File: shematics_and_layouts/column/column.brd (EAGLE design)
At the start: 160 x 100 mm, 1 part

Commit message: TASK: col shematic
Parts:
- removed U$1: RPI-ZERO, rpi-zero-without-test-pad:RASP_PI_ZERO_BOARD_FULL
- added A1: RPI-ZERO, rpi-zero-without-test-pad:RASP_PI_ZERO_BOARD_FULL
- added X1: (no value), con-conrad:733980-62
- added X2: (no value), con-berg:PN87520
- added X3: (no value), con-lsta:FE05-2
- added X5: LEDs, con-lstb:MA03-1
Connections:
- new net 3V3@1: A1.1, X3.5
- new net GND: X1.2, X1.3, X2.4, X5.3
- new net GND@3: A1.25, A1.39, A1.9
- new net GND@7: A1.14, A1.20, A1.30, A1.34, A1.6, X3.6
- new net N$1: A1.5, X3.2
- new net N$2: A1.3, X3.4
- new net N$3: A1.12, X5.2
- new net VCC: X1.1, X2.1, X5.1
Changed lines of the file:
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@@
 </autorouter>
 <elements>
-<element name="U$1" library="rpi-zero-without-test-pad" package="RASP_PI_ZERO_BOARD_FULL" value="RPI-ZERO" x="29.21" y="31.75"/>
+<element name="A1" library="rpi-zero-without-test-pad" package="RASP_PI_ZERO_BOARD_FULL" value="RPI-ZERO" x="-69.85" y="67.31"/>
+<element name="X1" library="con-conrad" package="733980-62" value="" x="3.81" y="-2.54"/>
+<element name="X2" library="con-berg" package="PN87520" value="" x="35.56" y="8.89">
+<attribute name="OC_NEWARK" value="unknown" x="35.56" y="8.89" size="1.778" layer="27" display="off"/>
+<attribute name="MPN" value="" x="35.56" y="8.89" size="1.778" layer="27" display="off"/>
+<attribute name="MF" value="" x="35.56" y="8.89" size="1.778" layer="27" display="off"/>
+<attribute name="OC_FARNELL" value="unknown" x="35.56" y="8.89" size="1.778" layer="27" display="off"/>
+</element>
+<element name="X3" library="con-lsta" package="FE05-2" value="" x="-24.13" y="44.45">
+<attribute name="OC_NEWARK" value="unknown" x="-24.13" y="44.45" size="1.778" layer="27" display="off"/>
+<attribute name="MPN" value="" x="-24.13" y="44.45" size="1.778" layer="27" display="off"/>
+<attribute name="MF" value="" x="-24.13" y="44.45" size="1.778" layer="27" display="off"/>
+<attribute name="OC_FARNELL" value="unknown" x="-24.13" y="44.45" size="1.778" layer="27" display="off"/>
+</element>
+<element name="X5" library="con-lstb" package="MA03-1" value="LEDs" x="-64.77" y="-11.43">
+<attribute name="OC_NEWARK" value="unknown" x="-64.77" y="-11.43" size="1.778" layer="27" display="off"/>
+<attribute name="MPN" value="" x="-64.77" y="-11.43" size="1.778" layer="27" display="off"/>
+<attribute name="MF" value="" x="-64.77" y="-11.43" size="1.778" layer="27" display="off"/>
+<attribute name="OC_FARNELL" value="unknown" x="-64.77" y="-11.43" size="1.778" layer="27" display="off"/>
+</element>
 </elements>
 <signals>
+<signal name="VCC">
+<contactref element="X1" pad="1"/>
+<contactref element="X2" pad="1"/>
+<contactref element="X5" pad="1"/>
+<wire x1="3.81" y1="6.03" x2="-67.31" y2="-11.43" width="0" layer="19" extent="1-1"/>
+<wire x1="32.06" y1="11.6" x2="3.81" y2="6.03" width="0" layer="19" extent="1-1"/>
+</signal>
+<signal name="GND">
+<contactref element="X1" pad="3"/>
+<contactref element="X1" pad="2"/>
+<contactref element="X2" pad="4"/>
+<contactref element="X5" pad="3"/>
+<wire x1="3.81" y1="-0.12" x2="-62.23" y2="-11.43" width="0" layer="19" extent="1-1"/>
+<wire x1="8.81" y1="3.03" x2="3.81" y2="-0.12" width="0" layer="19" extent="1-1"/>
+<wire x1="39.06" y1="11.6" x2="8.81" y2="3.03" width="0" layer="19" extent="1-1"/>
+</signal>
+<signal name="N$1">
+<contactref element="X3" pad="2"/>
+<contactref element="A1" pad="5"/>
+<wire x1="-56.4" y1="92.54" x2="-29.21" y2="43.18" width="0" layer="19" extent="1-1"/>
+</signal>
+<signal name="N$2">
+<contactref element="X3" pad="4"/>
+<contactref element="A1" pad="3"/>
+<wire x1="-58.94" y1="92.54" x2="-26.67" y2="43.18" width="0" layer="19" extent="1-1"/>
+</signal>
+<signal name="3V3@1">
+<contactref element="X3" pad="5"/>
+<contactref element="A1" pad="1"/>
+<wire x1="-61.48" y1="92.54" x2="-24.13" y2="45.72" width="0" layer="19" extent="1-1"/>
+</signal>
+<signal name="N$3">
+<contactref element="A1" pad="12"/>
+<contactref element="X5" pad="2"/>
+<wire x1="-48.78" y1="95.08" x2="-64.77" y2="-11.43" width="0" layer="19" extent="1-1"/>
+</signal>
+<signal name="GND@3">
+<contactref element="A1" pad="9"/>
+<contactref element="A1" pad="25"/>
+<contactref element="A1" pad="39"/>
+<wire x1="-31" y1="92.54" x2="-13.22" y2="92.54" width="0" layer="19" extent="1-1"/>
+<wire x1="-51.32" y1="92.54" x2="-31" y2="92.54" width="0" layer="19" extent="1-1"/>
+</signal>
+<signal name="GND@7">
+<contactref element="X3" pad="6"/>
+<contactref element="A1" pad="6"/>
+<contactref element="A1" pad="14"/>
+<contactref element="A1" pad="20"/>
+<contactref element="A1" pad="30"/>
+<contactref element="A1" pad="34"/>
+<wire x1="-25.92" y1="95.08" x2="-20.84" y2="95.08" width="0" layer="19" extent="1-1"/>
+<wire x1="-38.62" y1="95.08" x2="-25.92" y2="95.08" width="0" layer="19" extent="1-1"/>
+<wire x1="-46.24" y1="95.08" x2="-38.62" y2="95.08" width="0" layer="19" extent="1-1"/>
+<wire x1="-56.4" y1="95.08" x2="-46.24" y2="95.08" width="0" layer="19" extent="1-1"/>
+<wire x1="-24.13" y1="43.18" x2="-25.92" y2="95.08" width="0" layer="19" extent="1-1"/>
+</signal>
 </signals>
 </board>

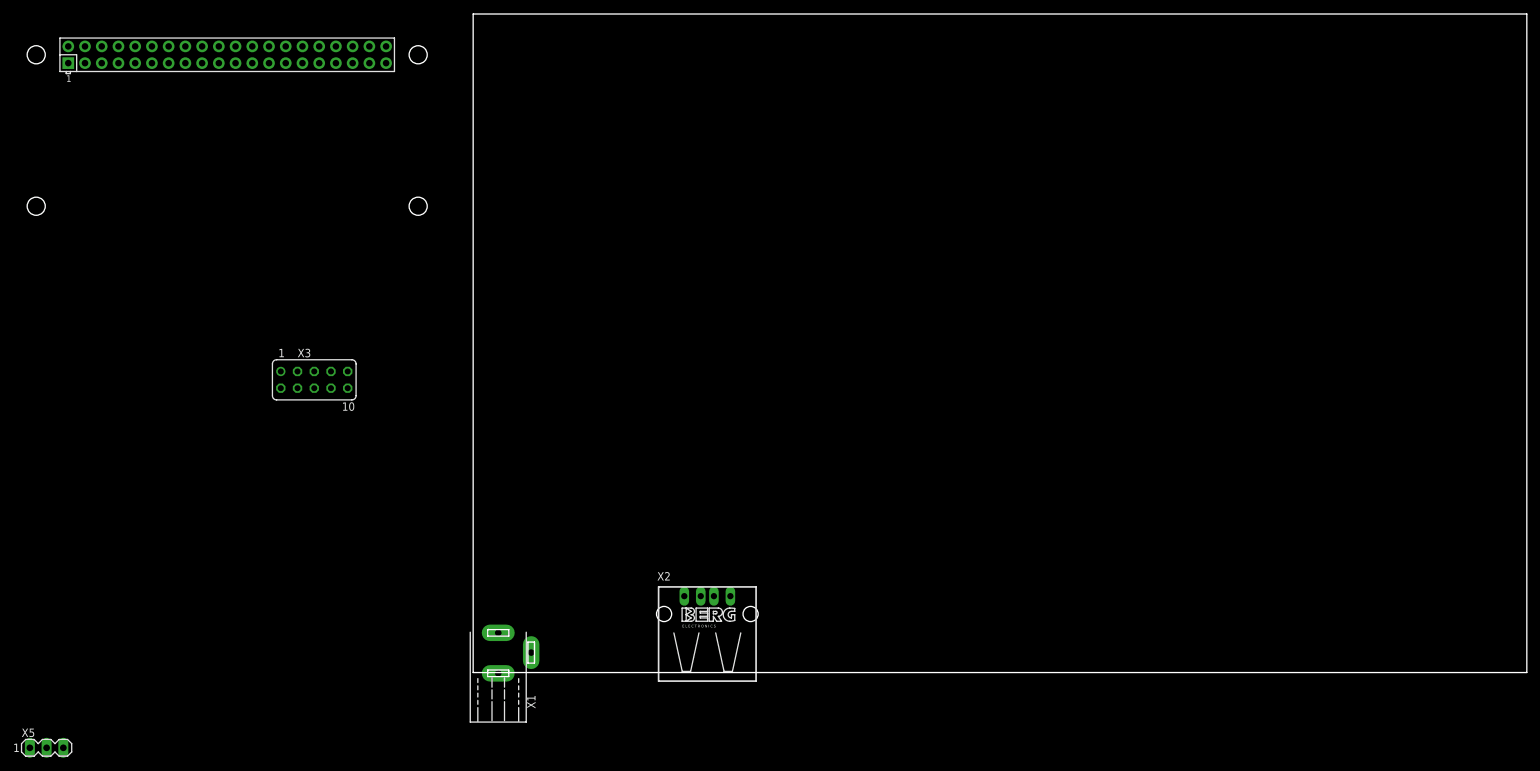
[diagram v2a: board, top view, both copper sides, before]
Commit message: TASK: col brd, part placement
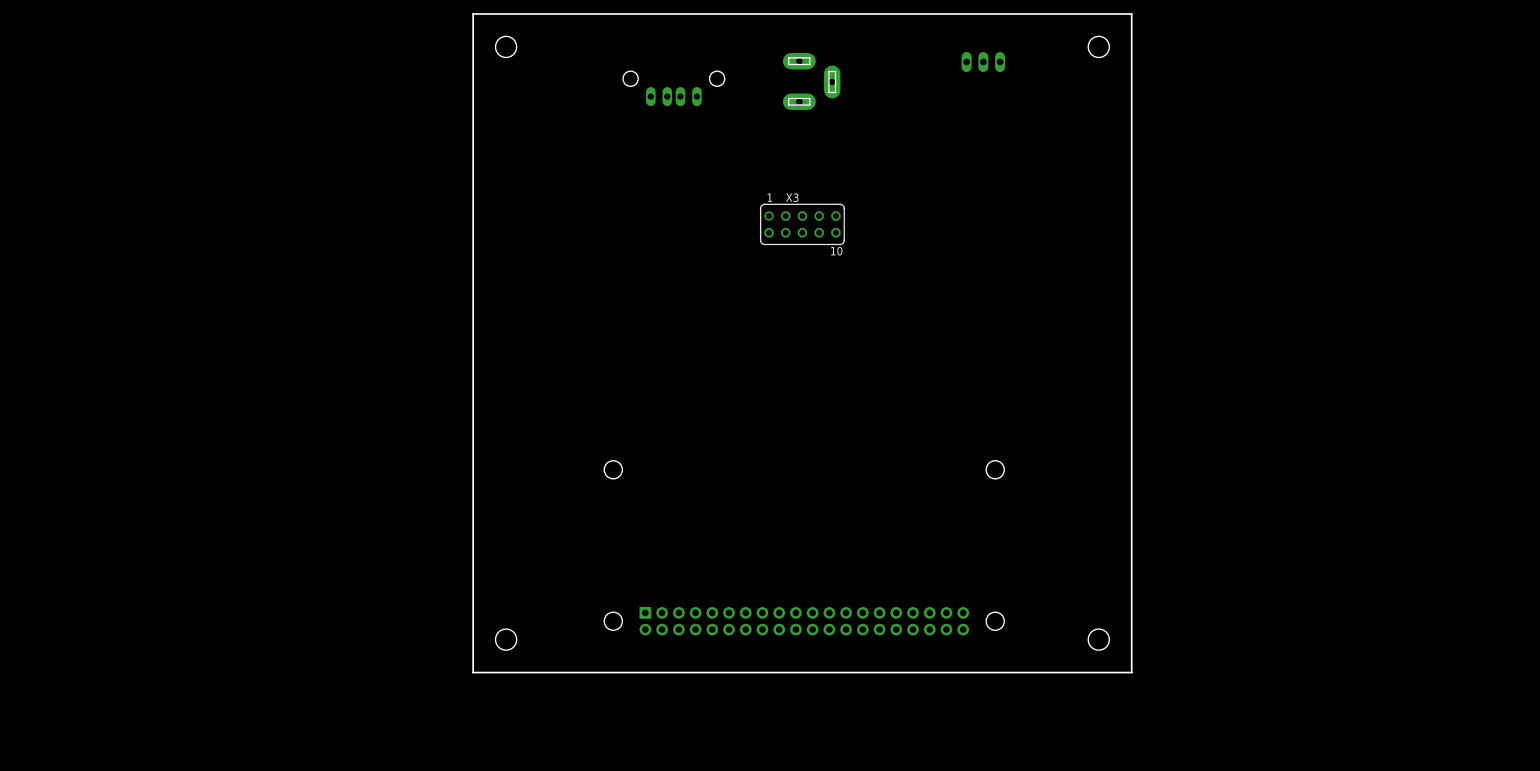
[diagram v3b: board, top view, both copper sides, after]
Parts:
- moved X5 176.3 mm to (77.5, 92.7), flipped to the bottom, turned to 180 degrees
- moved X1 108.0 mm to (49.5, 95.2), flipped to the bottom, turned to 180 degrees
- moved A1 93.6 mm to (17.8, 34.3), flipped to the bottom, turned to 180 degrees
- moved X2 81.4 mm to (30.5, 90.2), flipped to the bottom, turned to 180 degrees
- moved X3 77.8 mm to (50.0, 68.0)
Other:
- board size 160 x 100 mm -> 100 x 100 mm
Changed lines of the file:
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@@
 <layer number="43" name="vRestrict" color="2" fill="10" visible="yes" active="yes"/>
 <layer number="44" name="Drills" color="7" fill="1" visible="no" active="yes"/>
-<layer number="45" name="Holes" color="7" fill="1" visible="no" active="yes"/>
+<layer number="45" name="Holes" color="7" fill="1" visible="yes" active="yes"/>
 <layer number="46" name="Milling" color="3" fill="1" visible="no" active="yes"/>
 <layer number="47" name="Measures" color="7" fill="1" visible="no" active="yes"/>
@@
 <board>
 <plain>
-<wire x1="0" y1="0" x2="160" y2="0" width="0" layer="20"/>
-<wire x1="160" y1="0" x2="160" y2="100" width="0" layer="20"/>
-<wire x1="160" y1="100" x2="0" y2="100" width="0" layer="20"/>
-<wire x1="0" y1="100" x2="0" y2="0" width="0" layer="20"/>
+<wire x1="0" y1="0" x2="100" y2="0" width="0.254" layer="20"/>
+<wire x1="100" y1="0" x2="100" y2="100" width="0.254" layer="20"/>
+<wire x1="100" y1="100" x2="0" y2="100" width="0.254" layer="20"/>
+<wire x1="0" y1="100" x2="0" y2="0" width="0.254" layer="20"/>
+<hole x="5" y="95" drill="3.2"/>
+<hole x="95" y="95" drill="3.2"/>
+<hole x="95" y="5" drill="3.2"/>
+<hole x="5" y="5" drill="3.2"/>
 </plain>
 <attributes>
@@
 </autorouter>
 <elements>
-<element name="A1" library="rpi-zero-without-test-pad" package="RASP_PI_ZERO_BOARD_FULL" value="RPI-ZERO" x="-69.85" y="67.31"/>
-<element name="X1" library="con-conrad" package="733980-62" value="" x="3.81" y="-2.54"/>
-<element name="X2" library="con-berg" package="PN87520" value="" x="35.56" y="8.89">
-<attribute name="OC_NEWARK" value="unknown" x="35.56" y="8.89" size="1.778" layer="27" display="off"/>
-<attribute name="MPN" value="" x="35.56" y="8.89" size="1.778" layer="27" display="off"/>
-<attribute name="MF" value="" x="35.56" y="8.89" size="1.778" layer="27" display="off"/>
-<attribute name="OC_FARNELL" value="unknown" x="35.56" y="8.89" size="1.778" layer="27" display="off"/>
+<element name="A1" library="rpi-zero-without-test-pad" package="RASP_PI_ZERO_BOARD_FULL" value="RPI-ZERO" x="17.78" y="34.29" rot="MR180"/>
+<element name="X1" library="con-conrad" package="733980-62" value="" x="49.53" y="95.25" rot="MR180"/>
+<element name="X2" library="con-berg" package="PN87520" value="" x="30.48" y="90.17" rot="MR180">
+<attribute name="OC_NEWARK" value="unknown" x="30.48" y="90.17" size="1.778" layer="28" rot="MR180" display="off"/>
+<attribute name="MPN" value="" x="30.48" y="90.17" size="1.778" layer="28" rot="MR180" display="off"/>
+<attribute name="MF" value="" x="30.48" y="90.17" size="1.778" layer="28" rot="MR180" display="off"/>
+<attribute name="OC_FARNELL" value="unknown" x="30.48" y="90.17" size="1.778" layer="28" rot="MR180" display="off"/>
 </element>
-<element name="X3" library="con-lsta" package="FE05-2" value="" x="-24.13" y="44.45">
-<attribute name="OC_NEWARK" value="unknown" x="-24.13" y="44.45" size="1.778" layer="27" display="off"/>
-<attribute name="MPN" value="" x="-24.13" y="44.45" size="1.778" layer="27" display="off"/>
-<attribute name="MF" value="" x="-24.13" y="44.45" size="1.778" layer="27" display="off"/>
-<attribute name="OC_FARNELL" value="unknown" x="-24.13" y="44.45" size="1.778" layer="27" display="off"/>
+<element name="X3" library="con-lsta" package="FE05-2" value="" x="50" y="68.05">
+<attribute name="OC_NEWARK" value="unknown" x="50" y="68.05" size="1.778" layer="27" display="off"/>
+<attribute name="MPN" value="" x="50" y="68.05" size="1.778" layer="27" display="off"/>
+<attribute name="MF" value="" x="50" y="68.05" size="1.778" layer="27" display="off"/>
+<attribute name="OC_FARNELL" value="unknown" x="50" y="68.05" size="1.778" layer="27" display="off"/>
 </element>
-<element name="X5" library="con-lstb" package="MA03-1" value="LEDs" x="-64.77" y="-11.43">
-<attribute name="OC_NEWARK" value="unknown" x="-64.77" y="-11.43" size="1.778" layer="27" display="off"/>
-<attribute name="MPN" value="" x="-64.77" y="-11.43" size="1.778" layer="27" display="off"/>
-<attribute name="MF" value="" x="-64.77" y="-11.43" size="1.778" layer="27" display="off"/>
-<attribute name="OC_FARNELL" value="unknown" x="-64.77" y="-11.43" size="1.778" layer="27" display="off"/>
+<element name="X5" library="con-lstb" package="MA03-1" value="LEDs" x="77.47" y="92.71" rot="MR180">
+<attribute name="OC_NEWARK" value="unknown" x="77.47" y="92.71" size="1.778" layer="28" rot="MR180" display="off"/>
+<attribute name="MPN" value="" x="77.47" y="92.71" size="1.778" layer="28" rot="MR180" display="off"/>
+<attribute name="MF" value="" x="77.47" y="92.71" size="1.778" layer="28" rot="MR180" display="off"/>
+<attribute name="OC_FARNELL" value="unknown" x="77.47" y="92.71" size="1.778" layer="28" rot="MR180" display="off"/>
 </element>
 </elements>
@@
 <contactref element="X2" pad="1"/>
 <contactref element="X5" pad="1"/>
-<wire x1="3.81" y1="6.03" x2="-67.31" y2="-11.43" width="0" layer="19" extent="1-1"/>
-<wire x1="32.06" y1="11.6" x2="3.81" y2="6.03" width="0" layer="19" extent="1-1"/>
+<wire x1="49.53" y1="86.68" x2="74.93" y2="92.71" width="0" layer="19" extent="1-1"/>
+<wire x1="26.98" y1="87.46" x2="49.53" y2="86.68" width="0" layer="19" extent="1-1"/>
 </signal>
 <signal name="GND">
@@
 <contactref element="X2" pad="4"/>
 <contactref element="X5" pad="3"/>
-<wire x1="3.81" y1="-0.12" x2="-62.23" y2="-11.43" width="0" layer="19" extent="1-1"/>
-<wire x1="8.81" y1="3.03" x2="3.81" y2="-0.12" width="0" layer="19" extent="1-1"/>
-<wire x1="39.06" y1="11.6" x2="8.81" y2="3.03" width="0" layer="19" extent="1-1"/>
+<wire x1="49.53" y1="92.83" x2="80.01" y2="92.71" width="0" layer="19" extent="1-1"/>
+<wire x1="54.53" y1="89.68" x2="49.53" y2="92.83" width="0" layer="19" extent="1-1"/>
+<wire x1="33.98" y1="87.46" x2="54.53" y2="89.68" width="0" layer="19" extent="1-1"/>
 </signal>
 <signal name="N$1">
 <contactref element="X3" pad="2"/>
 <contactref element="A1" pad="5"/>
-<wire x1="-56.4" y1="92.54" x2="-29.21" y2="43.18" width="0" layer="19" extent="1-1"/>
+<wire x1="31.23" y1="9.06" x2="44.92" y2="66.78" width="0" layer="19" extent="1-1"/>
 </signal>
 <signal name="N$2">
 <contactref element="X3" pad="4"/>
 <contactref element="A1" pad="3"/>
-<wire x1="-58.94" y1="92.54" x2="-26.67" y2="43.18" width="0" layer="19" extent="1-1"/>
+<wire x1="28.69" y1="9.06" x2="47.46" y2="66.78" width="0" layer="19" extent="1-1"/>
 </signal>
 <signal name="3V3@1">
 <contactref element="X3" pad="5"/>
 <contactref element="A1" pad="1"/>
-<wire x1="-61.48" y1="92.54" x2="-24.13" y2="45.72" width="0" layer="19" extent="1-1"/>
+<wire x1="26.15" y1="9.06" x2="50" y2="69.32" width="0" layer="19" extent="1-1"/>
 </signal>
 <signal name="N$3">
 <contactref element="A1" pad="12"/>
 <contactref element="X5" pad="2"/>
-<wire x1="-48.78" y1="95.08" x2="-64.77" y2="-11.43" width="0" layer="19" extent="1-1"/>
+<wire x1="38.85" y1="6.52" x2="77.47" y2="92.71" width="0" layer="19" extent="1-1"/>
 </signal>
 <signal name="GND@3">
@@
 <contactref element="A1" pad="25"/>
 <contactref element="A1" pad="39"/>
-<wire x1="-31" y1="92.54" x2="-13.22" y2="92.54" width="0" layer="19" extent="1-1"/>
-<wire x1="-51.32" y1="92.54" x2="-31" y2="92.54" width="0" layer="19" extent="1-1"/>
+<wire x1="56.63" y1="9.06" x2="74.41" y2="9.06" width="0" layer="19" extent="1-1"/>
+<wire x1="36.31" y1="9.06" x2="56.63" y2="9.06" width="0" layer="19" extent="1-1"/>
 </signal>
 <signal name="GND@7">
@@
 <contactref element="A1" pad="30"/>
 <contactref element="A1" pad="34"/>
-<wire x1="-25.92" y1="95.08" x2="-20.84" y2="95.08" width="0" layer="19" extent="1-1"/>
-<wire x1="-38.62" y1="95.08" x2="-25.92" y2="95.08" width="0" layer="19" extent="1-1"/>
-<wire x1="-46.24" y1="95.08" x2="-38.62" y2="95.08" width="0" layer="19" extent="1-1"/>
-<wire x1="-56.4" y1="95.08" x2="-46.24" y2="95.08" width="0" layer="19" extent="1-1"/>
-<wire x1="-24.13" y1="43.18" x2="-25.92" y2="95.08" width="0" layer="19" extent="1-1"/>
+<wire x1="61.71" y1="6.52" x2="66.79" y2="6.52" width="0" layer="19" extent="1-1"/>
+<wire x1="49.01" y1="6.52" x2="61.71" y2="6.52" width="0" layer="19" extent="1-1"/>
+<wire x1="41.39" y1="6.52" x2="49.01" y2="6.52" width="0" layer="19" extent="1-1"/>
+<wire x1="31.23" y1="6.52" x2="41.39" y2="6.52" width="0" layer="19" extent="1-1"/>
+<wire x1="50" y1="66.78" x2="61.71" y2="6.52" width="0" layer="19" extent="1-1"/>
 </signal>
 </signals>
